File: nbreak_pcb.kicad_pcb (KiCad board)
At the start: 2 copper layers, 30.8 x 47.2 mm, 29 parts, among them J1 Conn_01x16, J2 Conn_01x05, Q1 BSS138, Q2 BSS138, U1 MAX485E, U2 MAX485E

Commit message: Fixed data polarity at DIN socket
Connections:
- SV1 pad 1: /Data- -> /Data+
- SV1 pad 4: /Data+ -> /Data-
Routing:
- net /Data-: track 26.4 -> 23.1 mm
- net /Data+: track 22.9 -> 25.4 mm
- net GND: vias 34 -> 35
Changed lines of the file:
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@@
 			(chamfer_ratio 0.2928932188)
 			(chamfer top_left top_right bottom_left bottom_right)
-			(net 23 "/Data-")
+			(net 20 "/Data+")
 			(pinfunction "1")
 			(pintype "passive")
@@
 			(chamfer_ratio 0.2928932188)
 			(chamfer top_left top_right bottom_left bottom_right)
-			(net 20 "/Data+")
+			(net 23 "/Data-")
 			(pinfunction "4")
 			(pintype "passive")
@@
 	)
 	(via
+		(at 100.75 49.9)
+		(size 0.6)
+		(drill 0.3)
+		(layers "F.Cu" "B.Cu")
+		(free yes)
+		(net 1)
+	)
+	(via
 		(at 87.3 55)
 		(size 0.6)
@@
 	)
 	(segment
-		(start 90 55.8)
-		(end 89.8 56)
-		(width 0.2)
-		(layer "F.Cu")
-		(net 20)
-	)
-	(segment
 		(start 80.431573 55.2)
 		(end 75.85 55.2)
@@
 	)
 	(segment
-		(start 89.5 61.5)
-		(end 89.5 56.714214)
+		(start 91.4 63.1)
+		(end 92 63.7)
 		(width 0.2)
 		(layer "B.Cu")
@@
 	)
 	(segment
-		(start 89.792893 56.007107)
-		(end 90 55.8)
+		(start 90 55.8)
+		(end 90.814214 56.614214)
+		(width 0.2)
+		(layer "B.Cu")
+		(net 20)
+	)
+	(segment
+		(start 91.4 58.028427)
+		(end 91.4 63.1)
 		(width 0.2)
 		(layer "B.Cu")
@@
 	)
 	(arc
-		(start 89.5 56.714214)
-		(mid 89.57612 56.331531)
-		(end 89.792893 56.007107)
+		(start 91.4 58.028427)
+		(mid 91.247759 57.26306)
+		(end 90.814214 56.614214)
 		(width 0.2)
 		(layer "B.Cu")
@@
 	)
 	(segment
-		(start 91.45 63.15)
-		(end 91.45 61.564214)
+		(start 79.510786 56.2)
+		(end 78.95 56.2)
 		(width 0.2)
 		(layer "F.Cu")
@@
 	)
 	(segment
-		(start 79.510786 56.2)
-		(end 78.95 56.2)
+		(start 88.914213 58.614213)
+		(end 87.3 57)
 		(width 0.2)
 		(layer "F.Cu")
@@
 	)
 	(segment
-		(start 92 63.7)
-		(end 91.45 63.15)
+		(start 87.3 57)
+		(end 83.3 57)
 		(width 0.2)
 		(layer "F.Cu")
@@
 	)
 	(segment
-		(start 87.3 57)
-		(end 83.3 57)
+		(start 89.5 61.5)
+		(end 89.5 60.028427)
 		(width 0.2)
 		(layer "F.Cu")
@@
 		(net 23)
 	)
-	(segment
-		(start 91.157107 60.857107)
-		(end 87.3 57)
-		(width 0.2)
-		(layer "F.Cu")
-		(net 23)
-	)
 	(arc
 		(start 83.192893 57.107107)
@@
 	)
 	(arc
-		(start 91.157107 60.857107)
-		(mid 91.37388 61.18153)
-		(end 91.45 61.564214)
+		(start 88.914213 58.614213)
+		(mid 89.347759 59.26306)
+		(end 89.5 60.028427)
 		(width 0.2)
 		(layer "F.Cu")

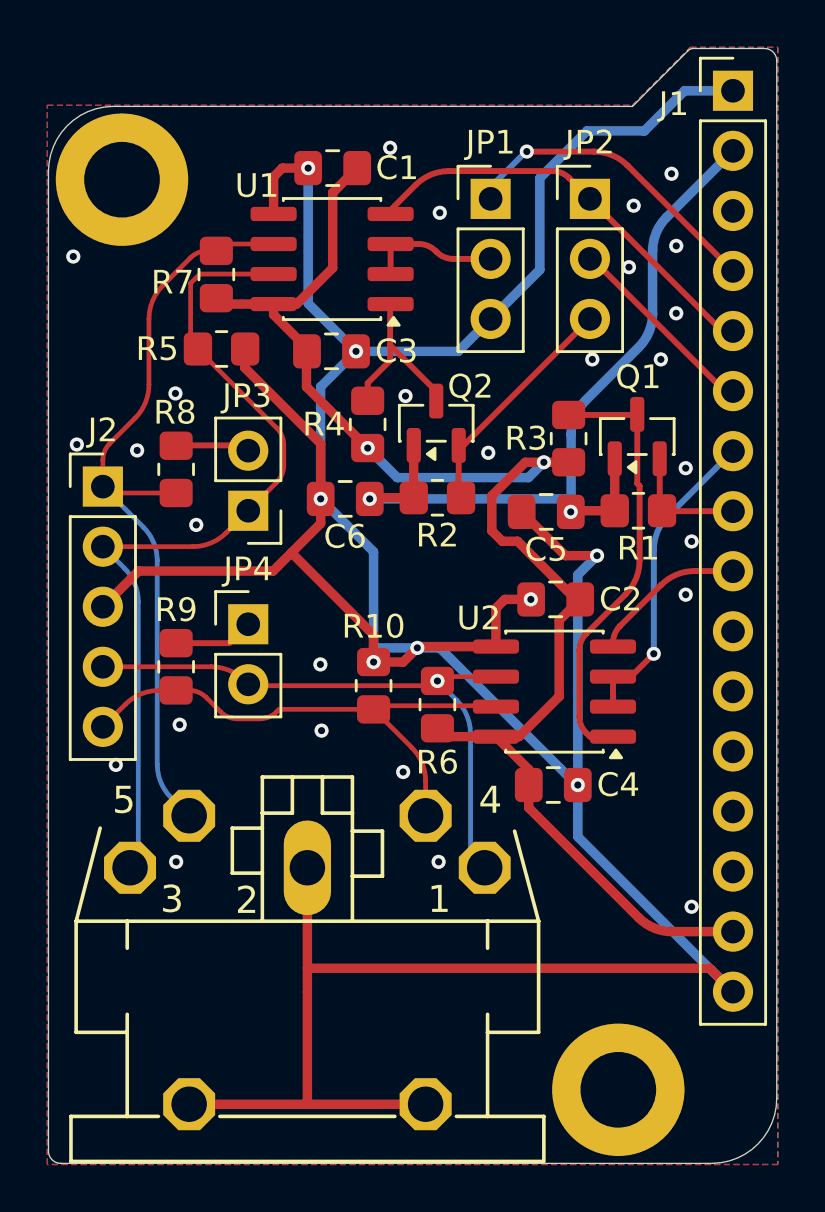
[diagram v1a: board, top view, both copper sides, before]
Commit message: Simplified clock and terminator selection
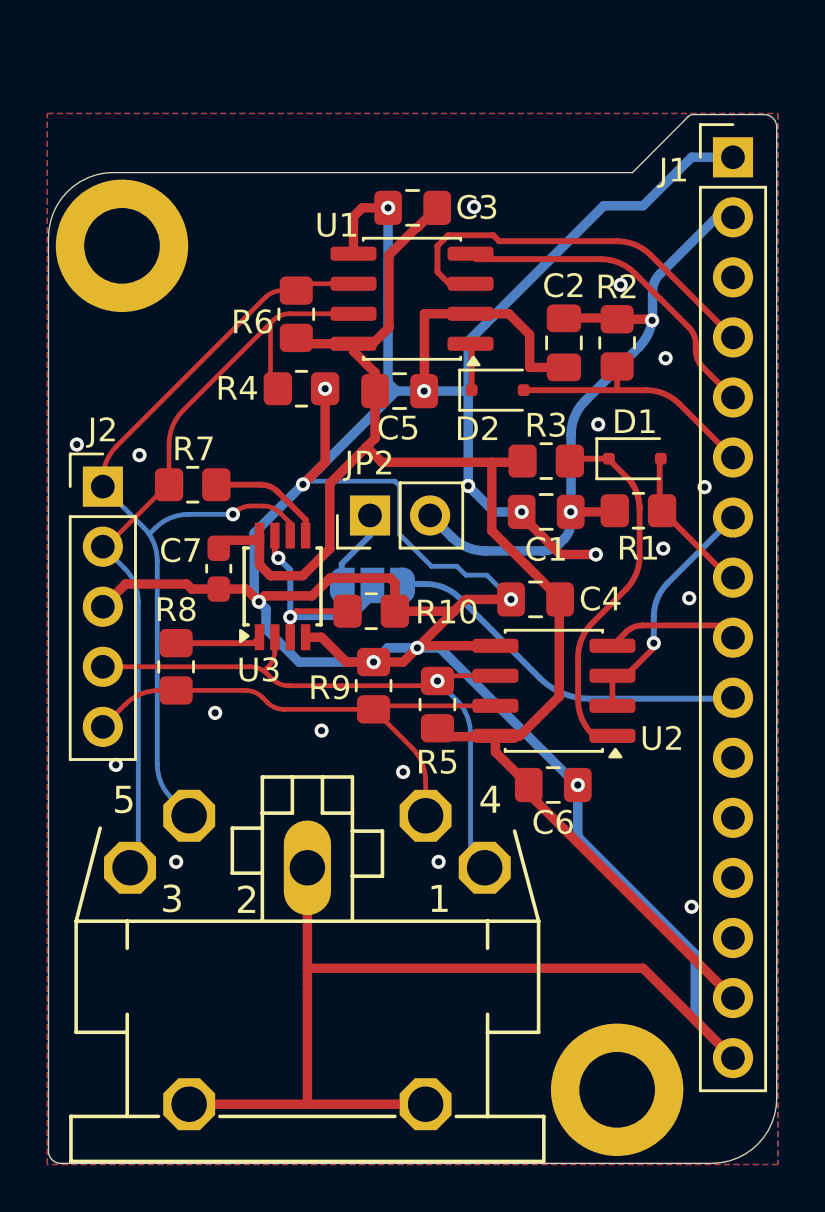
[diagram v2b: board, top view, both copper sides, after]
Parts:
- removed JP1: Jumper_3_Open, Connector_PinHeader_2.54mm:PinHeader_1x03_P2.54mm_Vertical
- removed the JP2 at (96.5, 35.4)
- removed JP4: Jumper_2_Open, Connector_PinHeader_2.54mm:PinHeader_1x02_P2.54mm_Vertical
- removed Q1, Q2: BSS138, Package_TO_SOT_SMD:SOT-23
- removed the R4 at (87.0, 45.0)
- added C7: 0.1uF, Capacitor_SMD:C_0603_1608Metric_Pad1.08x0.95mm_HandSolder, F.Cu at (80.8, 51.0)
- added D1: RB531VM, Diode_SMD:D_SOD-323F, F.Cu at (98.3, 46.4)
- added D2: RB531VM, Diode_SMD:D_SOD-323F, F.Cu at (92.5, 43.5)
- added JP3: Jumper_3_Open, Jumper:SolderJumper-3_P1.3mm_Open_RoundedPad1.0x1.5mm, B.Cu at (87.2, 51.8)
- added R10: 4K7, Resistor_SMD:R_0805_2012Metric_Pad1.20x1.40mm_HandSolder, F.Cu at (87.2, 52.9)
- added U3: 74AHC2G66, Package_SO:TSSOP-8_3x3mm_P0.65mm, F.Cu at (83.5, 51.8)
- R4: renamed from R5; value 1K0 -> 20K
- R6: renamed from R7; value 1K5 -> 20K
- R7: renamed from R8; value 120R -> 82R
- R8: renamed from R9; value 120R -> 82R
- moved C2 11.4 mm to (95.3, 41.5), turned to 90 degrees
- moved R2 10.0 mm to (97.6, 41.5), turned to -90 degrees
- moved JP2 5.15 mm to (87.2, 48.8), turned to 90 degrees
- moved C3 3.77 mm to (89.0, 35.8)
- moved R4 3.77 mm to (84.2, 43.4)
- moved R6 3.77 mm to (84.0, 40.3)
- moved U1 3.77 mm to (88.9, 39.6)
- moved C5 3.33 mm to (88.4, 43.5)
- moved J1 2.81 mm to (102.5, 33.6)
- moved REF** 2.80 mm to (76.7, 37.4)
- moved R3 1.34 mm to (94.6, 46.5), turned to 0 degrees
- moved R7 0.96 mm to (79.7, 47.5), turned to 180 degrees
- moved C4 0.85 mm to (94.2, 52.4)
- moved REF** 0.05 mm to (97.6, 73.1)
- renumbered C5 to C1, C6 to C2, C1 to C3, C2 to C4, C3 to C5, C4 to C6, JP3 to JP2, R6 to R5, R10 to R9
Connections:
- J1 pad 10: unconnected-(J1-Pin_10-Pad10) -> /IO8_Term_Sel
- JP2 pad 1: /Clk- -> Net-(JP2-A)
- JP2 pad 2: Net-(JP3-B) -> +3.3V
- R2 pad 2: Net-(JP2-B) -> /IO6_Clock_In
- R7 pad 1: /Clk+ -> Net-(R7-Pad1)
- R7 pad 2: Net-(JP3-B) -> /Clk-
- U1 pad 2: Net-(JP1-C) -> GND
- U1 pad 3: Net-(JP1-C) -> /IO4_Clock_OE
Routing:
- net GND: track 158.3 -> 182.7 mm, vias 35 -> 28
- net /IO8_Term_Sel: track 0.00 -> 15.7 mm
- net /Term: track 0.00 -> 11.5 mm, vias 0 -> 2
- net Net-(JP2-B): track 10.0 -> 0.00 mm
- net +3.3V: track 34.5 -> 28.7 mm
- net Net-(D2-K): track 7.66 -> 1.98 mm
- net Net-(JP1-C): track 5.66 -> 0.00 mm
- net Net-(R7-Pad1): track 0.00 -> 5.01 mm
- net +5V: track 61.3 -> 66.1 mm, vias 2 -> 0
- net /Clk+: track 33.2 -> 37.7 mm, vias 0 -> 1
- net /IO4_Clock_OE: track 13.4 -> 17.1 mm, vias 1 -> 0
- net Net-(JP2-A): track 0.00 -> 3.63 mm
- net /IO5_Clock_Out: track 18.0 -> 14.6 mm
- net Net-(JP3-B): track 3.15 -> 0.00 mm
- net /IO6_Clock_In: track 8.37 -> 11.4 mm
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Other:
- board size 30.8 x 47.2 mm -> 30.8 x 44.4 mm
- board text added: "D8"

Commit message: Added activity indicator LEDs
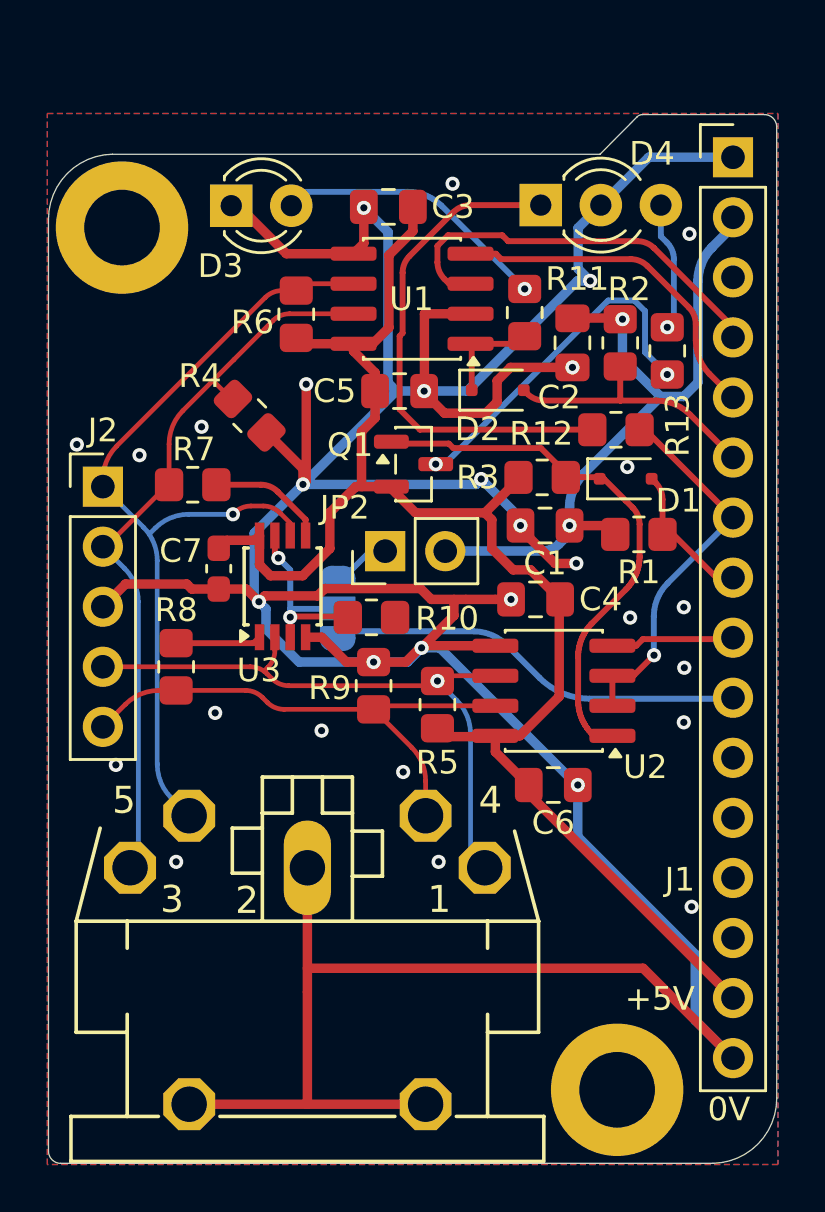
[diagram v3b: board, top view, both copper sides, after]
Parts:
- added D3: Blue, LED_THT:LED_D3.0mm, F.Cu at (81.3, 35.7)
- added D4: LED_Dual_AAK, LED_THT:LED_D3.0mm-3, F.Cu at (94.4, 35.7)
- added Q1: BSS84, Package_TO_SOT_SMD:SOT-23, F.Cu at (89.0, 46.6)
- added R11: 2K2, Resistor_SMD:R_0805_2012Metric_Pad1.20x1.40mm_HandSolder, F.Cu at (93.7, 40.2)
- added R12: 750R, Resistor_SMD:R_0805_2012Metric_Pad1.20x1.40mm_HandSolder, F.Cu at (97.5, 45.2)
- added R13: 1K2, Resistor_SMD:R_0805_2012Metric_Pad1.20x1.40mm_HandSolder, F.Cu at (99.7, 41.8)
- moved R4 2.47 mm to (82.1, 44.6), turned to 135 degrees
- moved JP3 1.76 mm to (85.8, 52.7), turned to 90 degrees
- moved JP2 1.64 mm to (87.8, 50.3)
- moved C3 1.03 mm to (87.9, 35.8)
- moved R1 1.00 mm to (98.5, 49.6)
- moved D1 0.94 mm to (98.0, 47.2)
- moved REF** 0.77 mm to (76.7, 36.6)
- moved R3 0.71 mm to (94.4, 47.2)
- moved C1 0.58 mm to (94.5, 49.2)
- moved C2 0.36 mm to (95.7, 41.5)
- moved R10 0.26 mm to (87.2, 53.1)
- moved R2 0.13 mm to (97.7, 41.5)
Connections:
- net Net-(D1-K) renamed /Dat_In
- net Net-(D2-K) renamed /Clk_FB
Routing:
- net Net-(D4-A1): track 0.00 -> 21.6 mm
- net Net-(Q1-D): track 0.00 -> 15.0 mm, vias 0 -> 2
- net Net-(D3-A): track 0.00 -> 11.7 mm, vias 0 -> 1
- net /Dat_In: track 15.7 -> 23.2 mm
- net Net-(D4-A2): track 0.00 -> 5.55 mm, vias 0 -> 1
- net /IO7_Data_OE: track 10.3 -> 15.8 mm
- net /Term: track 11.5 -> 9.04 mm
- net /Clk_FB: track 1.98 -> 4.43 mm
- net /IO8_Term_Sel: track 15.7 -> 17.8 mm
- net +3.3V: track 28.7 -> 30.4 mm
- net /Clk-: track 33.8 -> 32.1 mm
- net Net-(JP2-A): track 3.63 -> 2.47 mm
- net GND: track 182.7 -> 183.4 mm, vias 28 -> 31
- net +5V: track 66.1 -> 65.5 mm
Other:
- outline, holes or cut-outs redrawn

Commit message: Updates for version 2, following construction of first prototype
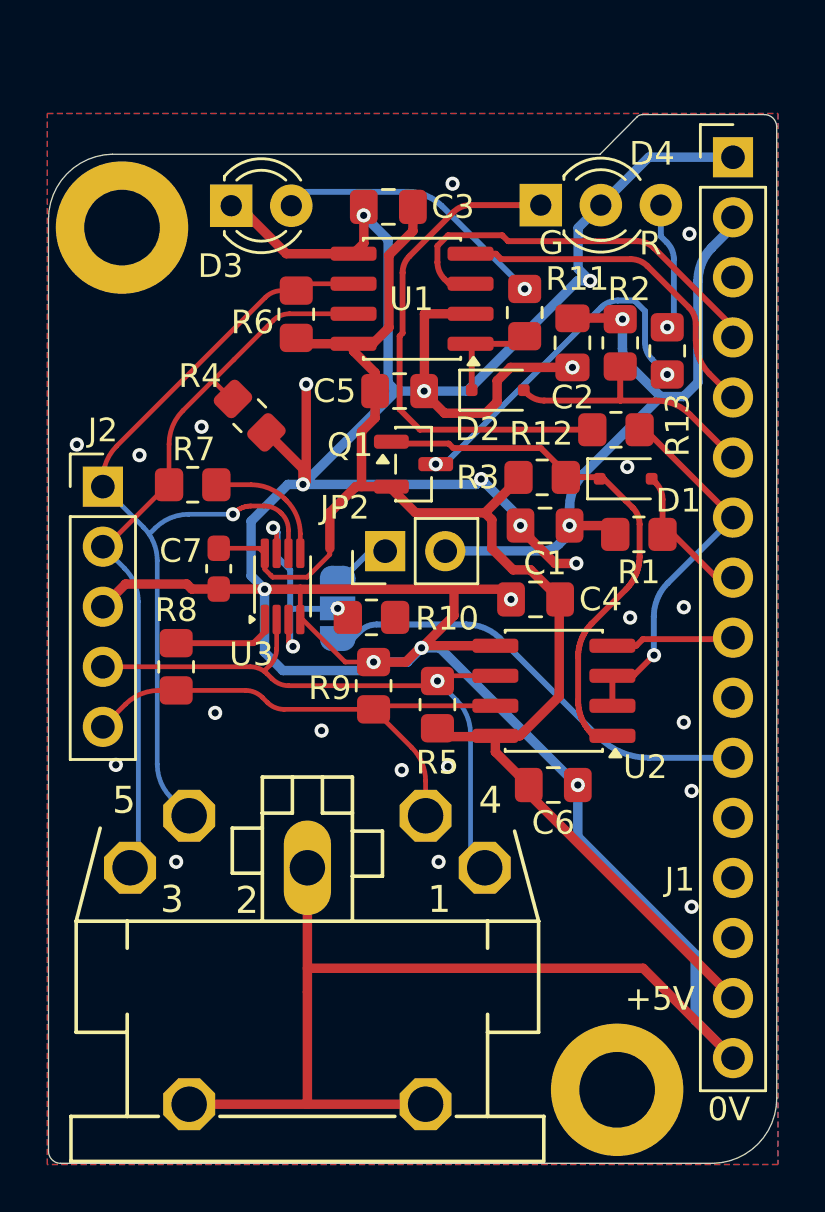
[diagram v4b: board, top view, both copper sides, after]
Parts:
- R12: value 750R -> 150R
- R13: value 1K2 -> 750R
- U3: value 74AHC2G66 -> 74LVC2G66DC; footprint Package_SO:TSSOP-8_3x3mm_P0.65mm -> Package_SO:VSSOP-8_2.3x2mm_P0.5mm
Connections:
- J1 pad 10: /IO8_Term_Sel -> unconnected-(J1-Pin_10-Pad10)
- J1 pad 11: unconnected-(J1-Pin_11-Pad11) -> /IO10_Term_Sel
- JP3 pad 1: /IO8_Term_Sel -> /IO10_Term_Sel
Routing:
- net /IO10_Term_Sel: track 0.00 -> 19.0 mm
- net /IO8_Term_Sel: track 17.8 -> 0.00 mm
- net GND: track 183.4 -> 186.3 mm, vias 31 -> 32
- net Net-(R8-Pad1): track 3.63 -> 4.47 mm
- net /Term: track 9.04 -> 9.87 mm, vias 2 -> 3
- net /Data+: track 26.9 -> 27.7 mm
- net /Clk+: track 37.7 -> 38.4 mm
- net +5V: track 65.5 -> 64.9 mm
- net Net-(R7-Pad1): track 5.01 -> 5.53 mm
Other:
- board text added: "D10"
- board text added: "G"
- board text added: "R"
- board text added: "V2.12 by Radiofan"
- board text removed: "V1.12 by Radiofan"
